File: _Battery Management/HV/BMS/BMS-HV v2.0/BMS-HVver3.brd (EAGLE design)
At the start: 152.4 x 124.8 mm, 416 parts, among them J3 M2S02B-PASK-2(LF)(SN), J4 M2S02B-PASK-2(LF)(SN), Q1 BSS308PE, Q10 BSS308PE, Q11 BSS308PE, Q12 BSS308PE, Q13 BSS308PE, Q14 BSS308PE, Q15 BSS308PE, Q16 BSS308PE, Q17 BSS308PE, Q18 BSS308PE, Q19 BSS308PE, Q2 BSS308PE, Q20 BSS308PE, Q21 BSS308PE, Q22 BSS308PE, Q23 BSS308PE, Q24 BSS308PE, Q25 BSS308PE, Q26 BSS308PE, Q27 BSS308PE, Q28 BSS308PE, Q29 BSS308PE, Q3 BSS308PE, Q30 BSS308PE, Q31 BSS308PE, Q32 BSS308PE, Q33 BSS308PE, Q34 BSS308PE, Q35 BSS308PE, Q36 BSS308PE, Q37 BSS308PE, Q38 BSS308PE, Q39 BSS308PE, Q4 BSS308PE, Q5 BSS308PE, Q6 BSS308PE, Q7 BSS308PE, Q8 BSS308PE, Q9 BSS308PE, U1 LTC6804-2, U2 LTC6804-2, U3 LTC6804-2

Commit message: 
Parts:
- added D37, D38, D39: LED_AMBER, FSAE Electric:CHIP_LED0805
- added R54, R55, R56: 1k, FSAE Electric:0603
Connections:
- new net N$120: D38.A, R55.1
- new net N$140: D39.A, R56.1
- net GPIO1: now also NTC8.2
- net GPIO10: now also D39.C
- net GPIO15: now also D37.C
- net GPIO2: now also NTC7.2
- net GPIO3: now also NTC6.2
- net GPIO4: now also NTC5.2
- net N$109: now also D37.A, R54.1; no longer NTC8.2
- net VREG: now also R55.2
- net VREG1: now also R56.2
- net VREG2: now also R54.2
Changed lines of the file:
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@@
 <element name="R52" library="adafruit" package="R2512" value="" x="102.3366" y="-24.892"/>
 <element name="R53" library="adafruit" package="R2512" value="" x="102.3366" y="-30.5054"/>
+<element name="R54" library="FSAE Electric" package="0603" value="1k" x="-74.93" y="-86.36">
+<attribute name="PARTNO" value="RC0603JR-071KL" x="-74.93" y="-73.66" size="1.778" layer="27" display="off"/>
+</element>
+<element name="D37" library="FSAE Electric" package="CHIP_LED0805" value="LED_AMBER" x="-73.66" y="-82.55">
+<attribute name="PARTNO" value="HSMA-C170" x="-81.28" y="-72.39" size="1.778" layer="27" display="off"/>
+</element>
+<element name="R55" library="FSAE Electric" package="0603" value="1k" x="-74.93" y="-102.87">
+<attribute name="PARTNO" value="RC0603JR-071KL" x="-74.93" y="-90.17" size="1.778" layer="27" display="off"/>
+</element>
+<element name="D38" library="FSAE Electric" package="CHIP_LED0805" value="LED_AMBER" x="-73.66" y="-99.06">
+<attribute name="PARTNO" value="HSMA-C170" x="-81.28" y="-88.9" size="1.778" layer="27" display="off"/>
+</element>
+<element name="R56" library="FSAE Electric" package="0603" value="1k" x="-74.93" y="-119.38">
+<attribute name="PARTNO" value="RC0603JR-071KL" x="-74.93" y="-106.68" size="1.778" layer="27" display="off"/>
+</element>
+<element name="D39" library="FSAE Electric" package="CHIP_LED0805" value="LED_AMBER" x="-73.66" y="-115.57">
+<attribute name="PARTNO" value="HSMA-C170" x="-81.28" y="-105.41" size="1.778" layer="27" display="off"/>
+</element>
 </elements>
 <signals>
@@
 <wire x1="14.467" y1="-7.766" x2="11.957" y2="-7.766" width="0.1778" layer="1"/>
 <wire x1="11.957" y1="-7.766" x2="11.303" y2="-7.112" width="0.1778" layer="1"/>
+<contactref element="NTC7" pad="2"/>
+<wire x1="7.8232" y1="-7.8884" x2="11.303" y2="-7.112" width="0" layer="19" extent="1-1"/>
 </signal>
 <signal name="N$175">
@@
 <wire x1="14.467" y1="-8.616" x2="11.41" y2="-8.616" width="0.1778" layer="1"/>
 <wire x1="11.41" y1="-8.616" x2="10.922" y2="-8.128" width="0.1778" layer="1"/>
+<contactref element="NTC8" pad="2"/>
+<wire x1="11.41" y1="-8.616" x2="8.001" y2="-42.8642" width="0" layer="19" extent="1-1"/>
 </signal>
 <signal name="VREF2">
@@
 <wire x1="14.467" y1="-6.116" x2="12.72" y2="-6.116" width="0.1778" layer="1"/>
 <wire x1="12.72" y1="-6.116" x2="12.192" y2="-5.588" width="0.1778" layer="1"/>
+<contactref element="NTC5" pad="2"/>
+<wire x1="9.262625" y1="6.513" x2="7.5946" y2="27.5446" width="0" layer="19" extent="1-1"/>
 </signal>
 <signal name="VREG">
@@
 <wire x1="15.9512" y1="9.6122" x2="18.0975" y2="9.6122" width="0.2286" layer="1"/>
 <wire x1="18.0975" y1="9.6122" x2="17.7419" y2="9.7138" width="0.2286" layer="1"/>
-<wire x1="13.208" y1="9.594" x2="13.7414" y2="14.478" width="0" layer="19" extent="1-1"/>
+<contactref element="R55" pad="2"/>
+<wire x1="8.259" y1="9.013" x2="-74.08" y2="-102.87" width="0" layer="19" extent="1-1"/>
+<wire x1="13.7414" y1="14.478" x2="13.208" y2="9.594" width="0" layer="19" extent="1-1"/>
 </signal>
 <signal name="A0">
@@
 <wire x1="14.467" y1="-6.966" x2="12.427" y2="-6.966" width="0.1778" layer="1"/>
 <wire x1="12.427" y1="-6.966" x2="11.684" y2="-6.223" width="0.1778" layer="1"/>
+<contactref element="NTC6" pad="2"/>
+<wire x1="9.262625" y1="5.013" x2="7.5438" y2="45.0706" width="0" layer="19" extent="1-1"/>
 </signal>
 <signal name="N$192">
@@
 <wire x1="64.643" y1="-23.7998" x2="64.643" y2="-26.3398" width="0.1778" layer="1"/>
 <wire x1="64.6176" y1="-26.3144" x2="64.643" y2="-26.3398" width="0.1778" layer="1"/>
-<wire x1="67.403225" y1="5.306" x2="63.782" y2="28.956" width="0" layer="19" extent="1-1"/>
-<wire x1="67.403225" y1="3.806" x2="67.403225" y2="5.306" width="0" layer="19" extent="1-1"/>
-<wire x1="68.8467" y1="2.5129" x2="67.403225" y2="3.806" width="0" layer="19" extent="1-16"/>
-<wire x1="65.0312" y1="-14.986" x2="68.8467" y2="2.5129" width="0" layer="19" extent="1-16"/>
-<wire x1="64.643" y1="-18.7198" x2="65.0312" y2="-14.986" width="0" layer="19" extent="1-1"/>
+<contactref element="R56" pad="2"/>
+<wire x1="64.643" y1="-26.3398" x2="-74.08" y2="-119.38" width="0" layer="19" extent="1-1"/>
+<wire x1="65.0312" y1="-14.986" x2="64.643" y2="-18.7198" width="0" layer="19" extent="1-1"/>
+<wire x1="68.8467" y1="2.5129" x2="65.0312" y2="-14.986" width="0" layer="19" extent="1-16"/>
+<wire x1="67.403225" y1="3.806" x2="68.8467" y2="2.5129" width="0" layer="19" extent="1-16"/>
+<wire x1="67.403225" y1="5.306" x2="67.403225" y2="3.806" width="0" layer="19" extent="1-1"/>
+<wire x1="63.782" y1="28.956" x2="67.403225" y2="5.306" width="0" layer="19" extent="1-1"/>
 </signal>
 <signal name="A4">
@@
 <contactref element="R66" pad="2"/>
 <contactref element="U1" pad="33"/>
-<wire x1="66.548" y1="-11.088" x2="67.403225" y2="1.806" width="0" layer="19" extent="1-1"/>
+<contactref element="D39" pad="C"/>
+<wire x1="66.548" y1="-11.088" x2="-73.66" y2="-114.52" width="0" layer="19" extent="1-1"/>
+<wire x1="67.403225" y1="1.806" x2="66.548" y2="-11.088" width="0" layer="19" extent="1-1"/>
 </signal>
 <signal name="SWTEN1">
@@
 <wire x1="-31.9532" y1="19.7612" x2="-31.9532" y2="17.0434" width="0.4064" layer="1"/>
 <wire x1="-31.9532" y1="17.0434" x2="-31.9532" y2="14.3256" width="0.4064" layer="1"/>
+<contactref element="R54" pad="2"/>
+<wire x1="-38.9018" y1="9.398" x2="-74.08" y2="-86.36" width="0" layer="19" extent="1-16"/>
 </signal>
 <signal name="A8">
@@
 <wire x1="-32.131" y1="7.1628" x2="-35.672575" y2="7.1628" width="0.1778" layer="1"/>
 <wire x1="-35.672575" y1="7.1628" x2="-35.695375" y2="7.14" width="0.1778" layer="1"/>
+<contactref element="D37" pad="C"/>
+<wire x1="-31.6484" y1="-2.5028" x2="-73.66" y2="-81.5" width="0" layer="19" extent="1-1"/>
 </signal>
 <signal name="SWTEN2">
@@
 <contactref element="J3" pad="2"/>
 <contactref element="J4" pad="2"/>
-<wire x1="74.4728" y1="33.02" x2="74.4728" y2="41.91" width="0" layer="19" extent="1-1"/>
-<wire x1="74.4728" y1="22.86" x2="74.4728" y2="33.02" width="0" layer="19" extent="1-1"/>
-<wire x1="36.5158" y1="-52.451" x2="74.4728" y2="22.86" width="0" layer="19" extent="1-1"/>
 <wire x1="39.0492" y1="52.9844" x2="39.0492" y2="51.1208" width="0.3048" layer="16"/>
 <wire x1="39.0492" y1="51.1208" x2="40.64" y2="49.53" width="0.3048" layer="16"/>
@@
 <wire x1="72.39" y1="41.91" x2="74.4728" y2="41.91" width="0.3048" layer="1"/>
 <wire x1="74.4728" y1="41.91" x2="74.93" y2="41.91" width="0.3048" layer="1"/>
+<wire x1="74.4728" y1="41.91" x2="74.4728" y2="33.02" width="0" layer="19" extent="1-1"/>
+<wire x1="74.4728" y1="22.86" x2="74.4728" y2="33.02" width="0" layer="19" extent="1-1"/>
+<wire x1="36.5158" y1="-52.451" x2="74.4728" y2="22.86" width="0" layer="19" extent="1-1"/>
 </signal>
 <signal name="N$129">
@@
 <contactref element="J3" pad="1"/>
 <contactref element="J4" pad="1"/>
+<wire x1="74.4728" y1="36.83" x2="72.39" y2="36.83" width="0.3048" layer="1"/>
+<wire x1="74.4728" y1="27.94" x2="74.4728" y2="36.83" width="0" layer="19" extent="1-1"/>
 <wire x1="74.4728" y1="17.78" x2="74.4728" y2="27.94" width="0" layer="19" extent="1-1"/>
-<wire x1="37.0492" y1="52.9844" x2="74.4728" y2="36.83" width="0" layer="19" extent="1-1"/>
+<wire x1="37.0492" y1="52.9844" x2="72.39" y2="36.83" width="0" layer="19" extent="1-1"/>
 <wire x1="38.5158" y1="-52.451" x2="74.4728" y2="17.78" width="0" layer="19" extent="1-1"/>
-<wire x1="74.4728" y1="36.83" x2="72.39" y2="36.83" width="0.3048" layer="1"/>
-<wire x1="72.39" y1="36.83" x2="74.4728" y2="27.94" width="0" layer="19" extent="1-16"/>
 </signal>
 <signal name="VREF1">
@@
 <via x="-4.6228" y="37.5158" extent="1-16" drill="0.5"/>
 <via x="-19.6088" y="40.3098" extent="1-16" drill="0.5"/>
-<contactref element="NTC5" pad="1"/>
 <contactref element="NTC6" pad="1"/>
 <contactref element="NTC7" pad="1"/>
+<contactref element="NTC5" pad="1"/>
 </signal>
 <signal name="GNDI">
@@
 </signal>
 <signal name="N$109">
-<contactref element="NTC8" pad="2"/>
+<contactref element="R54" pad="1"/>
+<contactref element="D37" pad="A"/>
+<wire x1="-73.66" y1="-83.6" x2="-75.78" y2="-86.36" width="0" layer="19" extent="1-1"/>
+</signal>
+<signal name="N$120">
+<contactref element="R55" pad="1"/>
+<contactref element="D38" pad="A"/>
+<wire x1="-73.66" y1="-100.11" x2="-75.78" y2="-102.87" width="0" layer="19" extent="1-1"/>
+</signal>
+<signal name="N$140">
+<contactref element="R56" pad="1"/>
+<contactref element="D39" pad="A"/>
+<wire x1="-73.66" y1="-116.62" x2="-75.78" y2="-119.38" width="0" layer="19" extent="1-1"/>
 </signal>
 </signals>

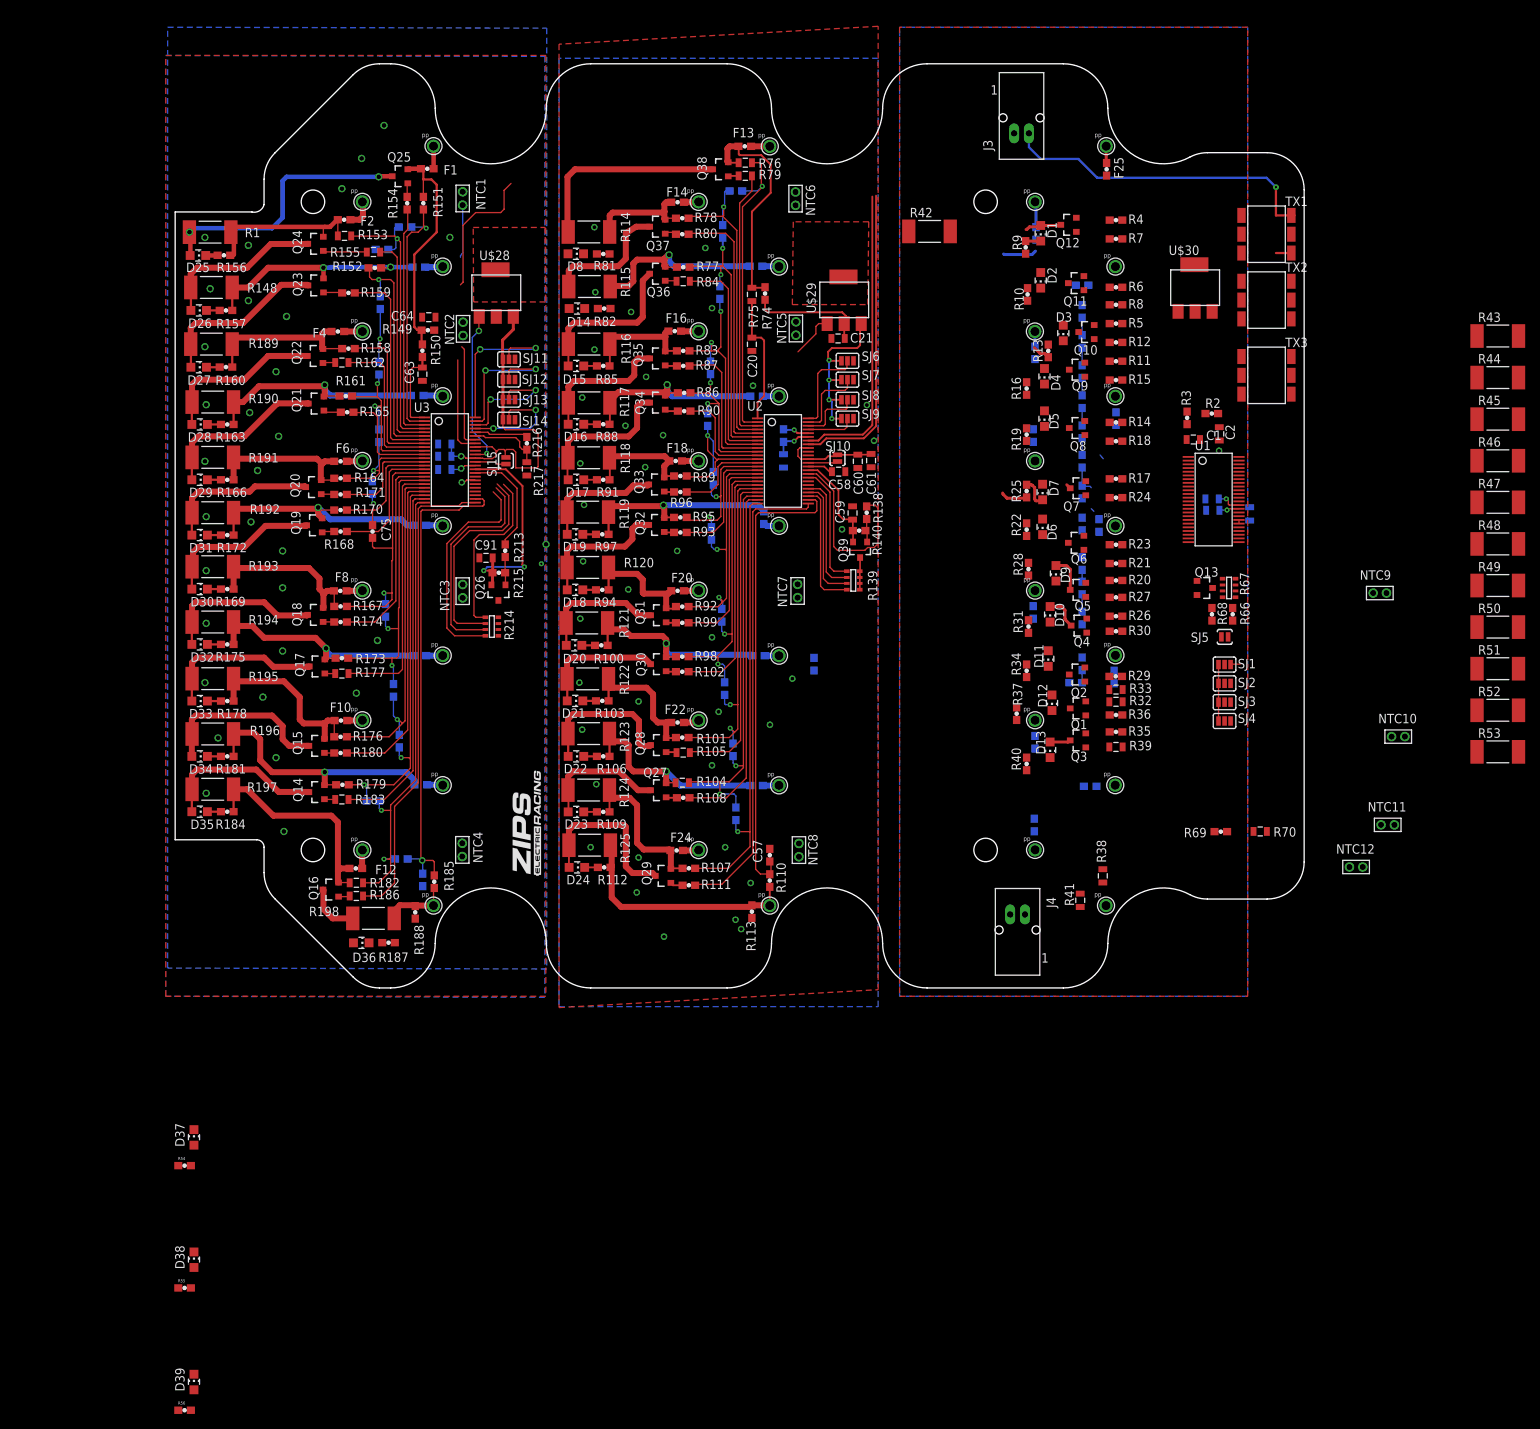
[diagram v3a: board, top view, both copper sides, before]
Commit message: 
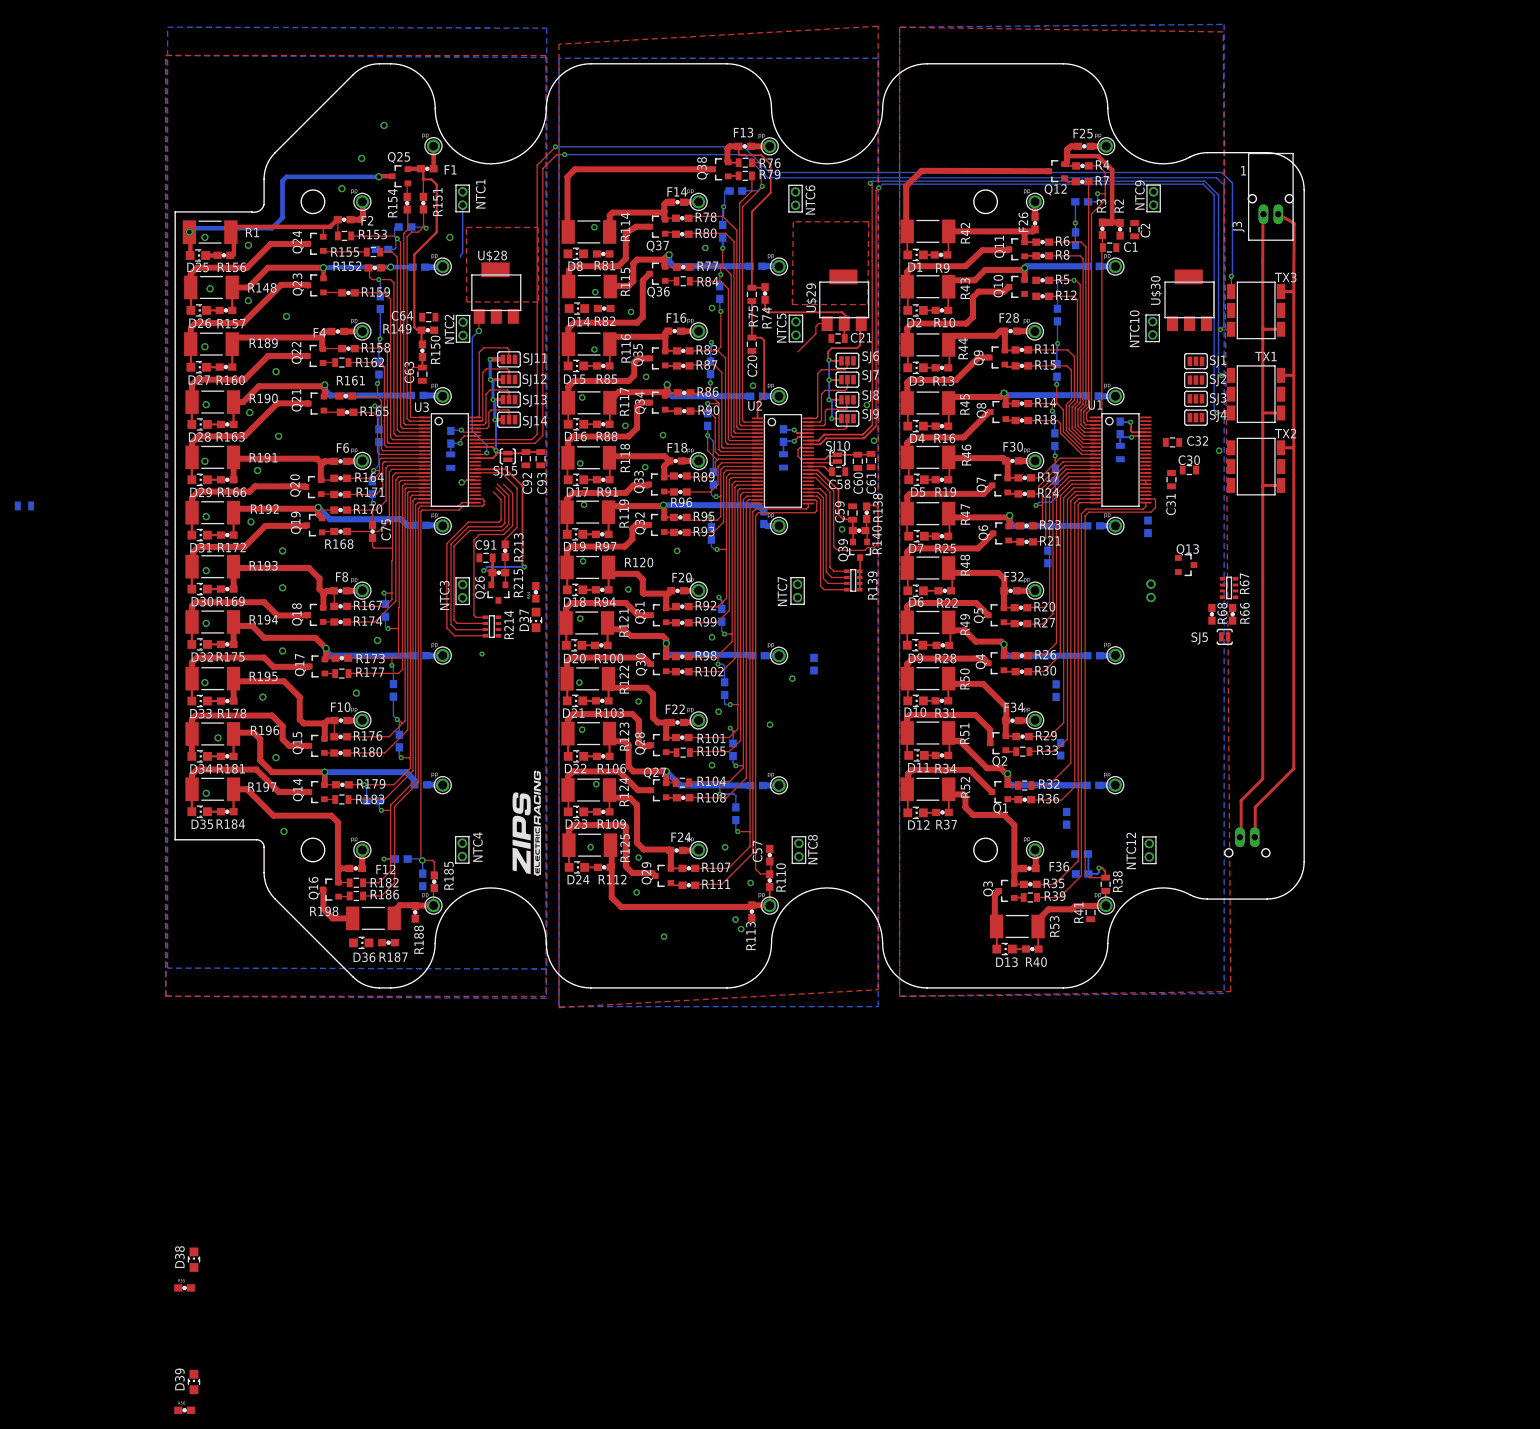
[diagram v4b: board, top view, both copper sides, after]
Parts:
- moved R54 90.8 mm to (-27.5, -8.97), turned to 90 degrees
- moved D37 83.7 mm to (-27.5, -12.7), turned to 180 degrees
- moved R52 77.6 mm to (25.4, -35.6), turned to 180 degrees
- moved R51 77.4 mm to (25.4, -28.0), turned to 180 degrees
- moved R50 77.2 mm to (25.4, -20.6), turned to 180 degrees
- moved R43 77.2 mm to (25.4, 32.3), turned to 180 degrees
- moved R49 77.1 mm to (25.4, -13.0), turned to 180 degrees
- moved R44 77.0 mm to (25.4, 24.4), turned to 180 degrees
- moved R48 77.0 mm to (25.4, -5.69), turned to 180 degrees
- moved R45 76.9 mm to (25.4, 16.6), turned to 180 degrees
- moved R47 76.9 mm to (25.4, 1.65), turned to 180 degrees
- moved R46 76.9 mm to (25.4, 9.25), turned to 180 degrees
- moved R53 69.0 mm to (37.5, -54.1), turned to 180 degrees
- moved NTC10 64.3 mm to (55.8, 26.7), turned to 90 degrees
- moved NTC9 61.4 mm to (55.9, 44.2), turned to 90 degrees
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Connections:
- net GPIO5: now also D38.C
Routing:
- net IPA2: track 14.0 -> 156.6 mm, vias 0 -> 2
- net IMA2: track 31.9 -> 161.4 mm, vias 0 -> 2
- net N$129: track 2.08 -> 93.2 mm
- net IMA: track 41.3 -> 120.0 mm, vias 0 -> 2
- net IPA: track 40.4 -> 116.0 mm, vias 0 -> 2
- net C23: track 1.69 -> 70.3 mm, vias 0 -> 1
- net S24: track 0.00 -> 65.7 mm
- net C21: track 0.00 -> 57.4 mm
- net N$125: track 43.8 -> 92.8 mm, vias 1 -> 0
- net S23: track 0.00 -> 48.4 mm
- net C20: track 2.36 -> 45.6 mm
- net S22: track 0.00 -> 42.4 mm
- net C13: track 0.00 -> 41.6 mm, vias 0 -> 1
- net C19: track 1.60 -> 40.6 mm
- net C14: track 2.36 -> 38.4 mm, vias 0 -> 1
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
